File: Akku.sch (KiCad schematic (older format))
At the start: 47 parts, among them P1 CONN_02X10, P2 CONN_02X10, P3 CONN_02X10, SW1 SWITCH_INV, SW2 SWITCH_INV, SW3 SWITCH_INV, U1 7400, U2 7408, U3 4069, U4 74LS193, U5 74LS541, U6 74LS193, U7 74LS540

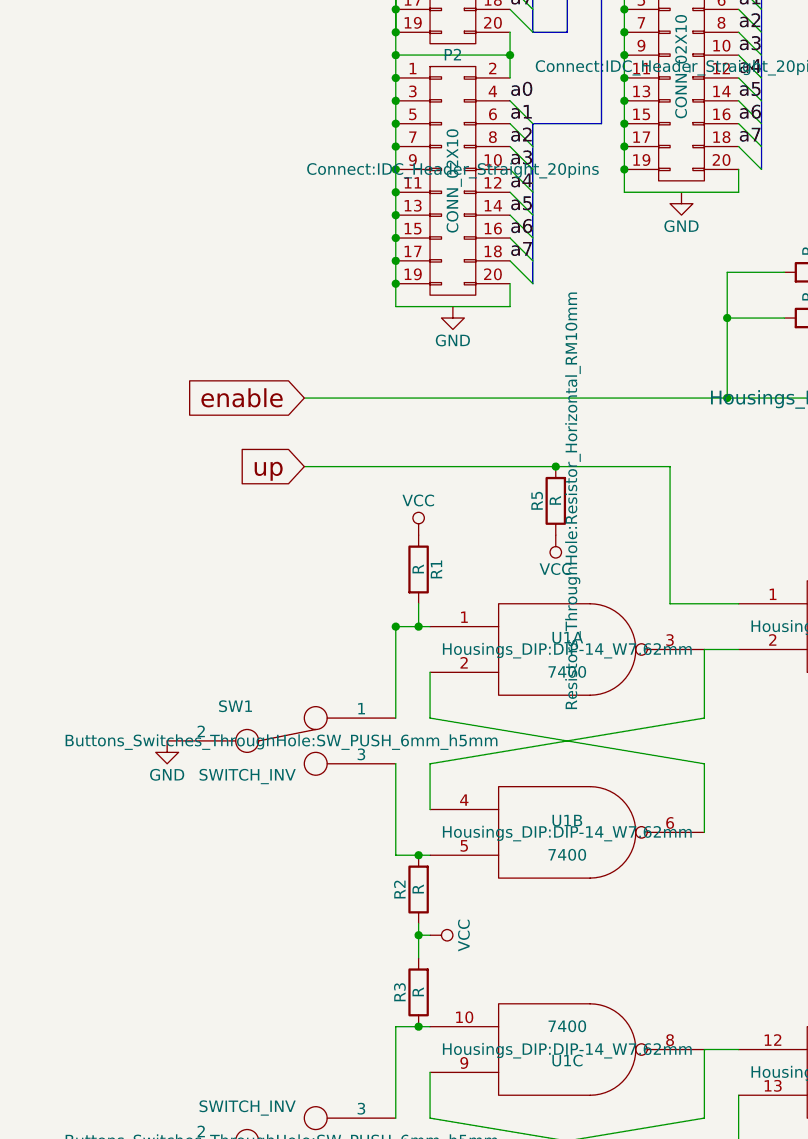
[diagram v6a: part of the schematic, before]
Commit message: einige Footprints geändert
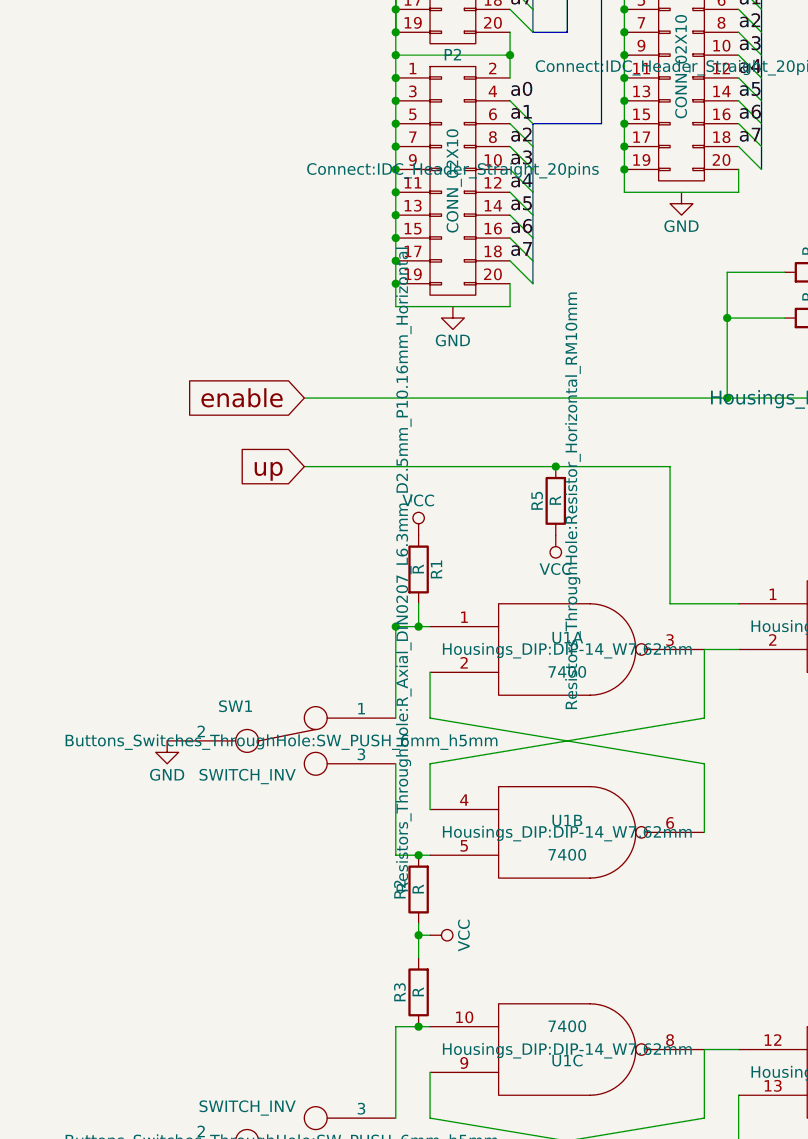
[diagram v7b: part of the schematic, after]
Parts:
- R1: footprint (none) -> Resistors_ThroughHole:R_Axial_DIN0207_L6.3mm_D2.5mm_P10.16mm_Horizontal
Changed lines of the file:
@@
 F 0 "R1" V 2080 3850 50  0000 C CNN
 F 1 "R" V 2000 3850 50  0000 C CNN
-F 2 "" V 1930 3850 50  0000 C CNN
+F 2 "Resistors_ThroughHole:R_Axial_DIN0207_L6.3mm_D2.5mm_P10.16mm_Horizontal" V 1930 3850 50  0000 C CNN
 F 3 "" H 2000 3850 50  0000 C CNN
 	1    2000 3850

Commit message: Akku.sch verändert, Components ausgetauscht
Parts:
- removed unit 6 of U3
- removed unit 5 of U3
- removed unit 1 of U3
- removed unit 4 of U3
- added U? (x4): 74HC14, symbol 74HC14
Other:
- note added: "November 2017\n"
- note removed: "26.09.2016"
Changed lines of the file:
@@
 Comment4 ""
 $EndDescr
-Text Notes 7350 7500 0    60   ~ 0
+Text Notes 7400 7500 0    60   ~ 0
 Akku/PC - Modul
 Text Notes 8150 7650 0    60   ~ 0
-26.09.2016
+November 2017\n
 Text Notes 7050 6850 0    197  ~ 0
 Akkumulator
@@
 CLR
 $Comp
-L 4069 U3
-U 6 1 57E980E6
-P 8650 5250
-F 0 "U3" V 8604 5428 50  0000 L CNN
-F 1 "4069" V 8695 5428 50  0000 L CNN
-F 2 "" H 8650 5250 60  0000 C CNN
-F 3 "" H 8650 5250 60  0001 C CNN
-	6    8650 5250
-	0    1    1    0
-$EndComp
-$Comp
 L R R14
 U 1 1 57E98213
@@
 	1    9500 5100
 	-1   0    0    1
-$EndComp
-$Comp
-L 4069 U3
-U 5 1 57F2FBE5
-P 5700 2650
-F 0 "U3" V 5654 2828 50  0000 L CNN
-F 1 "4069" V 5745 2828 50  0000 L CNN
-F 2 "" H 5700 2650 60  0000 C CNN
-F 3 "" H 5700 2650 60  0001 C CNN
-	5    5700 2650
-	0    1    -1   0
 $EndComp
 $Comp
@@
 $Comp
 L 4069 U3
-U 1 1 580F1100
-P 4150 3100
-F 0 "U3" V 4104 3278 50  0000 L CNN
-F 1 "4069" V 4195 3278 50  0000 L CNN
-F 2 "Housings_DIP:DIP-14_W7.62mm_LongPads" H 4150 3100 60  0000 C CNN
-F 3 "" H 4150 3100 60  0001 C CNN
-	1    4150 3100
-	1    0    0    1
-$EndComp
-$Comp
-L 4069 U3
 U 2 1 580F11C5
 P 5050 3100
@@
 F 3 "" H 900 6350 50  0000 C CNN
 	1    900  6350
-	1    0    0    -1
-$EndComp
-$Comp
-L 4069 U3
-U 4 1 58105168
-P 5200 6050
-F 0 "U3" V 5154 6228 50  0000 L CNN
-F 1 "4069" V 5245 6228 50  0000 L CNN
-F 2 "" H 5200 6050 60  0000 C CNN
-F 3 "" H 5200 6050 60  0001 C CNN
-	4    5200 6050
 	1    0    0    -1
 $EndComp
@@
 NoConn ~ 9700 4250
 NoConn ~ 9700 4450
+$Comp
+L 74HC14 U?
+U 1 1 5A159C74
+P 4150 3100
+F 0 "U?" H 4300 3200 50  0000 C CNN
+F 1 "74HC14" H 4350 3000 50  0000 C CNN
+F 2 "" H 4150 3100 50  0000 C CNN
+F 3 "" H 4150 3100 50  0000 C CNN
+	1    4150 3100
+	1    0    0    -1
+$EndComp
+$Comp
+L 74HC14 U?
+U 1 1 5A159ED2
+P 5700 2650
+F 0 "U?" H 5850 2750 50  0000 C CNN
+F 1 "74HC14" H 5900 2550 50  0000 C CNN
+F 2 "" H 5700 2650 50  0000 C CNN
+F 3 "" H 5700 2650 50  0000 C CNN
+	1    5700 2650
+	0    -1   -1   0
+$EndComp
+$Comp
+L 74HC14 U?
+U 1 1 5A15A24E
+P 5200 6050
+F 0 "U?" H 5350 6150 50  0000 C CNN
+F 1 "74HC14" H 5400 5950 50  0000 C CNN
+F 2 "" H 5200 6050 50  0000 C CNN
+F 3 "" H 5200 6050 50  0000 C CNN
+	1    5200 6050
+	1    0    0    -1
+$EndComp
+$Comp
+L 74HC14 U?
+U 1 1 5A15A4DE
+P 8650 5250
+F 0 "U?" H 8800 5350 50  0000 C CNN
+F 1 "74HC14" H 8850 5150 50  0000 C CNN
+F 2 "" H 8650 5250 50  0000 C CNN
+F 3 "" H 8650 5250 50  0000 C CNN
+	1    8650 5250
+	0    1    1    0
+$EndComp
 $EndSCHEMATC
